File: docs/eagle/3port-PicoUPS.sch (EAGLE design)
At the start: 51 parts, among them IC1 MAX471CPA, IC2 MAX471CPA, IC3 MAX471CPA, IC5 7805TV, K1 APF30212C, K2 APF30212C, K3 APF30212C, Q1 MMBT2222A, Q2 MMBT2222A, Q3 MMBT2222A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

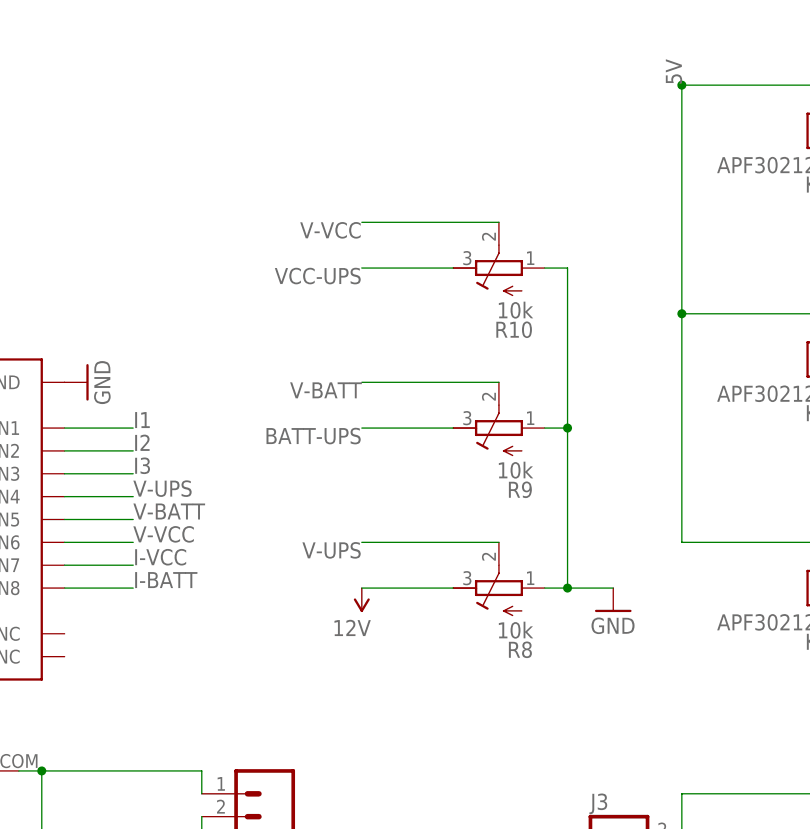
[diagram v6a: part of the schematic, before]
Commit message: Replace potis with fixed voltage dividers at 3k9 : 1k each which will give me 24.5V of range. 15V input will now read 3.061V on the ADC inputs.
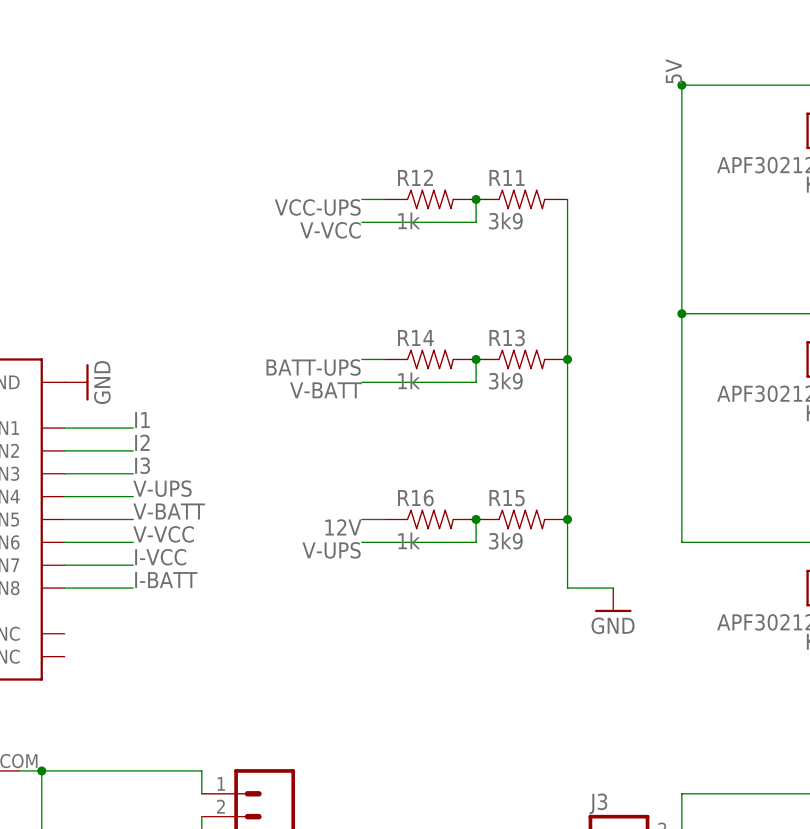
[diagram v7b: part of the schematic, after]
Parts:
- removed R10, R8, R9: 10k, rcl:R-TRIMM3296W
- added R11, R13, R15: 3k9, SparkFun-Passives:RESISTOR0805-RES
- added R12, R14, R16: 1k, SparkFun-Passives:RESISTOR0805-RES
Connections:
- net 12V: now also R16.1; no longer R8.E
- net BATT-UPS: now also R14.1; no longer R9.E
- net GND: now also R11.2, R13.2, R15.2; no longer R10.A, R8.A, R9.A
- net V-BATT: now also R13.1, R14.2; no longer R9.S
- net V-UPS: now also R15.1, R16.2; no longer R8.S
- net V-VCC: now also R11.1, R12.2; no longer R10.S
- net VCC-UPS: now also R12.1; no longer R10.E
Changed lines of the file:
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@@
 <part name="D1" library="SparkFun-LED" deviceset="LED-BLUE" device="0603" value="BLUE"/>
 <part name="GND2" library="SparkFun-Aesthetics" deviceset="GND" device=""/>
-<part name="SUPPLY2" library="SparkFun-Aesthetics" deviceset="12V" device=""/>
 <part name="SUPPLY3" library="SparkFun-Aesthetics" deviceset="12V" device=""/>
 <part name="GND3" library="SparkFun-Aesthetics" deviceset="GND" device=""/>
@@
 <part name="D3" library="SparkFun-LED" deviceset="LED-GREEN" device="0603" value="GREEN"/>
 <part name="D4" library="SparkFun-LED" deviceset="LED-GREEN" device="0603" value="GREEN"/>
-<part name="R8" library="rcl" deviceset="R-TRIMM" device="3296W" value="10k"/>
 <part name="GND12" library="SparkFun-Aesthetics" deviceset="GND" device=""/>
 <part name="GND7" library="SparkFun-Aesthetics" deviceset="GND" device=""/>
@@
 <part name="GND14" library="SparkFun-Aesthetics" deviceset="GND" device=""/>
 <part name="GND15" library="SparkFun-Aesthetics" deviceset="GND" device=""/>
-<part name="R9" library="rcl" deviceset="R-TRIMM" device="3296W" value="10k"/>
-<part name="R10" library="rcl" deviceset="R-TRIMM" device="3296W" value="10k"/>
 <part name="J1" library="SparkFun-Connectors" deviceset="M04" device="PTH"/>
 <part name="GND16" library="SparkFun-Aesthetics" deviceset="GND" device=""/>
@@
 <part name="J8" library="SparkFun-Connectors" deviceset="M02" device="5MM"/>
 <part name="J9" library="SparkFun-Connectors" deviceset="M02" device="5MM"/>
+<part name="R12" library="SparkFun-Passives" deviceset="RESISTOR" device="0805-RES" value="1k"/>
+<part name="R11" library="SparkFun-Passives" deviceset="RESISTOR" device="0805-RES" value="3k9"/>
+<part name="R13" library="SparkFun-Passives" deviceset="RESISTOR" device="0805-RES" value="3k9"/>
+<part name="R14" library="SparkFun-Passives" deviceset="RESISTOR" device="0805-RES" value="1k"/>
+<part name="R15" library="SparkFun-Passives" deviceset="RESISTOR" device="0805-RES" value="3k9"/>
+<part name="R16" library="SparkFun-Passives" deviceset="RESISTOR" device="0805-RES" value="1k"/>
 </parts>
 <sheets>
@@
 <instance part="D1" gate="G$1" x="5.08" y="10.16"/>
 <instance part="GND2" gate="1" x="223.52" y="91.44"/>
-<instance part="SUPPLY2" gate="G$1" x="195.58" y="93.98" rot="R180"/>
 <instance part="SUPPLY3" gate="G$1" x="25.4" y="78.74"/>
 <instance part="GND3" gate="1" x="25.4" y="68.58"/>
@@
 <instance part="D3" gate="G$1" x="114.3" y="55.88" rot="R270"/>
 <instance part="D4" gate="G$1" x="165.1" y="55.88" rot="R270"/>
-<instance part="R8" gate="G$1" x="210.82" y="93.98" rot="R90"/>
 <instance part="GND12" gate="1" x="48.26" y="91.44"/>
 <instance part="GND7" gate="1" x="48.26" y="60.96"/>
@@
 <instance part="GND14" gate="1" x="256.54" y="73.66" rot="R180"/>
 <instance part="GND15" gate="1" x="256.54" y="33.02" rot="R180"/>
-<instance part="R9" gate="G$1" x="210.82" y="111.76" rot="R90"/>
-<instance part="R10" gate="G$1" x="210.82" y="129.54" rot="R90"/>
 <instance part="J1" gate="G$1" x="106.68" y="99.06"/>
 <instance part="GND16" gate="1" x="114.3" y="86.36"/>
@@
 <instance part="J8" gate="G$1" x="134.62" y="71.12" rot="R180"/>
 <instance part="J9" gate="G$1" x="83.82" y="71.12" rot="R180"/>
+<instance part="R12" gate="G$1" x="203.2" y="137.16"/>
+<instance part="R11" gate="G$1" x="213.36" y="137.16"/>
+<instance part="R13" gate="G$1" x="213.36" y="119.38"/>
+<instance part="R14" gate="G$1" x="203.2" y="119.38"/>
+<instance part="R15" gate="G$1" x="213.36" y="101.6"/>
+<instance part="R16" gate="G$1" x="203.2" y="101.6"/>
 </instances>
 <busses>
@@
 <junction x="154.94" y="35.56"/>
 <pinref part="SUPPLY6" gate="G$1" pin="12V"/>
-</segment>
-<segment>
-<pinref part="R8" gate="G$1" pin="E"/>
-<pinref part="SUPPLY2" gate="G$1" pin="12V"/>
-<wire x1="205.74" y1="93.98" x2="195.58" y2="93.98" width="0.1524" layer="91"/>
 </segment>
 <segment>
@@
 <wire x1="22.86" y1="76.2" x2="25.4" y2="76.2" width="0.1524" layer="91"/>
 <wire x1="25.4" y1="76.2" x2="25.4" y2="78.74" width="0.1524" layer="91"/>
+</segment>
+<segment>
+<pinref part="R16" gate="G$1" pin="1"/>
+<wire x1="198.12" y1="101.6" x2="195.58" y2="101.6" width="0.1524" layer="91"/>
+<label x="195.58" y="101.6" size="1.778" layer="95" rot="R180"/>
 </segment>
 </net>
@@
 </segment>
 <segment>
-<pinref part="R8" gate="G$1" pin="A"/>
 <pinref part="GND2" gate="1" pin="GND"/>
-<wire x1="215.9" y1="93.98" x2="218.44" y2="93.98" width="0.1524" layer="91"/>
 <wire x1="218.44" y1="93.98" x2="223.52" y2="93.98" width="0.1524" layer="91"/>
-<wire x1="218.44" y1="93.98" x2="218.44" y2="111.76" width="0.1524" layer="91"/>
-<junction x="218.44" y="93.98"/>
-<pinref part="R9" gate="G$1" pin="A"/>
-<wire x1="218.44" y1="111.76" x2="215.9" y2="111.76" width="0.1524" layer="91"/>
-<wire x1="218.44" y1="111.76" x2="218.44" y2="129.54" width="0.1524" layer="91"/>
-<junction x="218.44" y="111.76"/>
-<pinref part="R10" gate="G$1" pin="A"/>
-<wire x1="218.44" y1="129.54" x2="215.9" y2="129.54" width="0.1524" layer="91"/>
+<wire x1="218.44" y1="93.98" x2="218.44" y2="101.6" width="0.1524" layer="91"/>
+<wire x1="218.44" y1="101.6" x2="218.44" y2="119.38" width="0.1524" layer="91"/>
+<pinref part="R13" gate="G$1" pin="2"/>
+<junction x="218.44" y="119.38"/>
+<pinref part="R15" gate="G$1" pin="2"/>
+<junction x="218.44" y="101.6"/>
+<pinref part="R11" gate="G$1" pin="2"/>
+<wire x1="218.44" y1="137.16" x2="218.44" y2="119.38" width="0.1524" layer="91"/>
 </segment>
 <segment>
@@
 <net name="V-UPS" class="0">
 <segment>
-<wire x1="210.82" y1="99.06" x2="195.58" y2="99.06" width="0.1524" layer="91"/>
 <label x="195.58" y="99.06" size="1.778" layer="95" rot="R180"/>
-<pinref part="R8" gate="G$1" pin="S"/>
+<pinref part="R15" gate="G$1" pin="1"/>
+<pinref part="R16" gate="G$1" pin="2"/>
+<wire x1="208.28" y1="99.06" x2="195.58" y2="99.06" width="0.1524" layer="91"/>
+<wire x1="208.28" y1="101.6" x2="208.28" y2="99.06" width="0.1524" layer="91"/>
+<junction x="208.28" y="101.6"/>
 </segment>
 <segment>
@@
 </segment>
 <segment>
-<pinref part="R10" gate="G$1" pin="E"/>
-<wire x1="205.74" y1="129.54" x2="195.58" y2="129.54" width="0.1524" layer="91"/>
-<label x="195.58" y="129.54" size="1.778" layer="95" rot="R180"/>
+<pinref part="R12" gate="G$1" pin="1"/>
+<wire x1="198.12" y1="137.16" x2="195.58" y2="137.16" width="0.1524" layer="91"/>
+<label x="195.58" y="137.16" size="1.778" layer="95" rot="R180"/>
 </segment>
 </net>
@@
 <net name="BATT-UPS" class="0">
 <segment>
-<pinref part="R9" gate="G$1" pin="E"/>
-<wire x1="205.74" y1="111.76" x2="195.58" y2="111.76" width="0.1524" layer="91"/>
-<label x="195.58" y="111.76" size="1.778" layer="95" rot="R180"/>
-</segment>
-<segment>
 <pinref part="U$2" gate="G$1" pin="IP-@3"/>
 <pinref part="U$2" gate="G$1" pin="IP-@4"/>
@@
 <wire x1="243.84" y1="7.62" x2="231.14" y2="7.62" width="0.1524" layer="91"/>
 </segment>
+<segment>
+<pinref part="R14" gate="G$1" pin="1"/>
+<wire x1="198.12" y1="119.38" x2="195.58" y2="119.38" width="0.1524" layer="91"/>
+<label x="195.58" y="119.38" size="1.778" layer="95" rot="R180"/>
+</segment>
 </net>
 <net name="V-BATT" class="0">
 <segment>
-<pinref part="R9" gate="G$1" pin="S"/>
-<wire x1="210.82" y1="116.84" x2="195.58" y2="116.84" width="0.1524" layer="91"/>
 <label x="195.58" y="116.84" size="1.778" layer="95" rot="R180"/>
+<pinref part="R13" gate="G$1" pin="1"/>
+<pinref part="R14" gate="G$1" pin="2"/>
+<wire x1="208.28" y1="116.84" x2="195.58" y2="116.84" width="0.1524" layer="91"/>
+<wire x1="208.28" y1="119.38" x2="208.28" y2="116.84" width="0.1524" layer="91"/>
+<junction x="208.28" y="119.38"/>
 </segment>
 <segment>
@@
 <net name="V-VCC" class="0">
 <segment>
-<pinref part="R10" gate="G$1" pin="S"/>
-<wire x1="210.82" y1="134.62" x2="195.58" y2="134.62" width="0.1524" layer="91"/>
-<label x="195.58" y="134.62" size="1.778" layer="95" rot="R180"/>
-</segment>
-<segment>
 <pinref part="U1" gate="U1" pin="AN6"/>
 <wire x1="162.56" y1="99.06" x2="170.18" y2="99.06" width="0.1524" layer="91"/>
 <label x="170.18" y="99.06" size="1.778" layer="95"/>
 </segment>
-</net>
+<segment>
+<label x="195.58" y="134.62" size="1.778" layer="95" rot="R180"/>
+<pinref part="R12" gate="G$1" pin="2"/>
+<pinref part="R11" gate="G$1" pin="1"/>
+<wire x1="208.28" y1="134.62" x2="195.58" y2="134.62" width="0.1524" layer="91"/>
+<wire x1="208.28" y1="137.16" x2="208.28" y2="134.62" width="0.1524" layer="91"/>
+<junction x="208.28" y="137.16"/>
+</segment>
+</net>
